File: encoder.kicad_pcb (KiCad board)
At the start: 2 copper layers, 22 x 23.9 mm, 13 parts, among them P1 Molex PicoBlade 6 Right, U1 TLE5012B

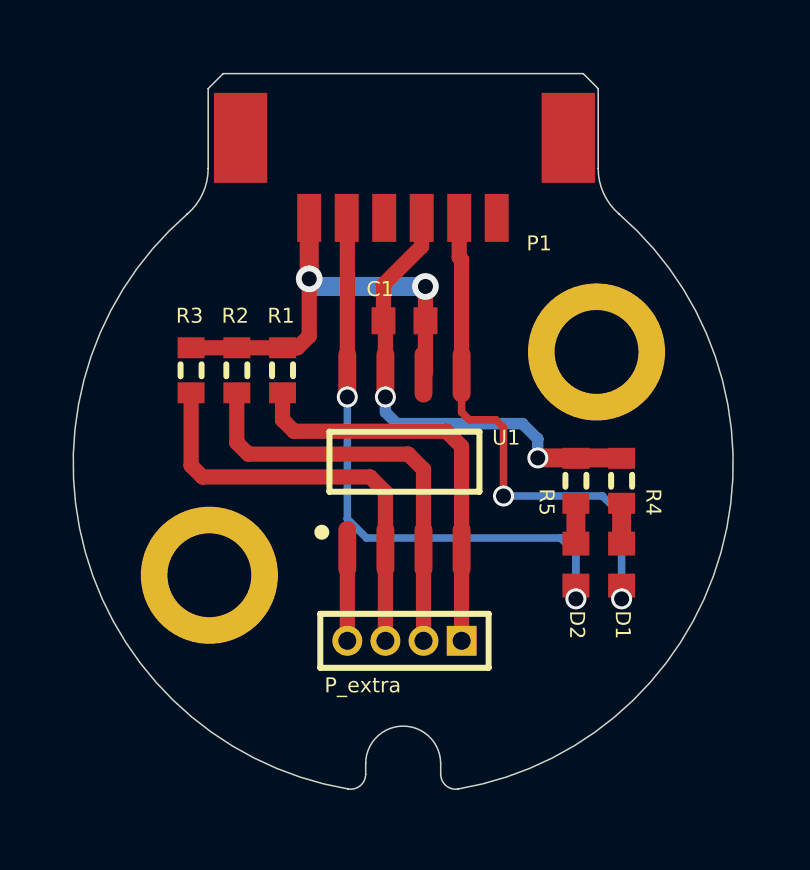
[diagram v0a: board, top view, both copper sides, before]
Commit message: Move to kicad symbols, route INC_C to the main connector.
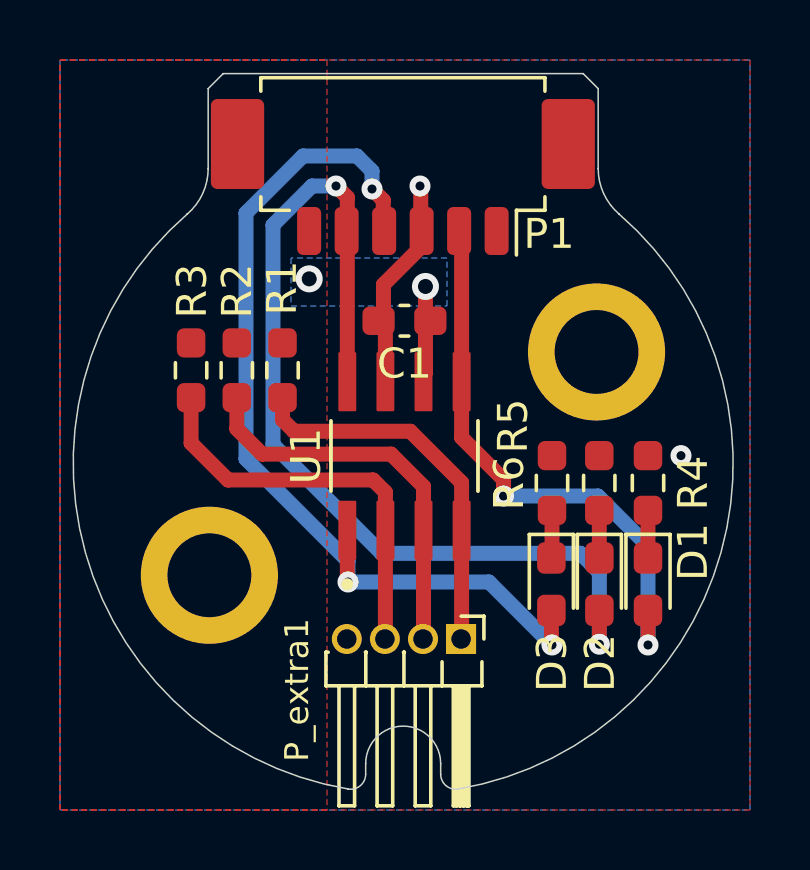
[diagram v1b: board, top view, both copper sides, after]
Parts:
- removed the ? at (142.0, 109.8)
- removed the ? at (154.9, 102.4)
- removed P_extra: MHDR1X4, Miscellaneous Connectors.IntLib:MHDR1X4
- added ?: , , F.Cu at (142.2, 110.1)
- added ?: , , F.Cu at (155.0, 102.4)
- added D3: RED_LED, LED_SMD:LED_0603_1608Metric_Pad1.05x0.95mm_HandSolder, F.Cu at (153.4, 110.1)
- added P_extra1: MHDR1X4, Connector_PinHeader_1.27mm:PinHeader_1x04_P1.27mm_Horizontal, F.Cu at (150.4, 111.9)
- added R6: 1K, Resistor_SMD:R_0603_1608Metric_Pad0.98x0.95mm_HandSolder, F.Cu at (153.5, 106.7)
- C1: value Cap Semi -> 100nF; footprint Miscellaneous Devices.IntLib:1608[0603] -> Capacitor_SMD:C_0603_1608Metric_Pad1.08x0.95mm_HandSolder
- D1, D2: footprint Miscellaneous Devices.IntLib:1608[0603] -> LED_SMD:LED_0603_1608Metric_Pad1.05x0.95mm_HandSolder
- P1: footprint ImmPCB2.IntLib:Molex PicoBlade 6 Right SMD -> 532610671:Molex_PicoBlade_53261-0671_1x06-1MP_P1.25mm_Horizontal
- R1, R2, R3: value Res3 -> 2.2K; footprint Miscellaneous Devices.IntLib:J1-0603 -> Resistor_SMD:R_0603_1608Metric_Pad0.98x0.95mm_HandSolder
- R4, R5: value Res3 -> 1K; footprint Miscellaneous Devices.IntLib:J1-0603 -> Resistor_SMD:R_0603_1608Metric_Pad0.98x0.95mm_HandSolder
- U1: footprint MagneticEncoder.IntLib:SO-8 -> TLE5012BE9000XUMA1:SOIC127P600X175-8N
- moved P1 3.69 mm to (148.5, 95.9), turned to 180 degrees
- moved D1 1.10 mm to (156.7, 110.1), turned to -90 degrees
- moved D2 1.02 mm to (155.0, 110.1), turned to -90 degrees
- moved R4 0.88 mm to (156.7, 106.7)
- moved R5 0.78 mm to (155.0, 106.7)
- moved U1 0.19 mm to (148.5, 105.8)
- turned C1 to 180 degrees
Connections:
- net CSQ renamed /CSQ
- net DATA renamed /DATA
- net SCK renamed /SCK
- C1 pad 1: GND -> +5V
- C1 pad 2: VCC -> GND
- D1 pad 1: INC_A -> Net-(D1-K)
- D1 pad 2: NetD1_2 -> /INC_A
- D2 pad 1: INC_B -> Net-(D2-K)
- D2 pad 2: NetD2_2 -> /INC_B
- P1 pad 1: VCC -> unconnected-(P1-Pin_1-Pad1)
- P1 pad 2: INC_B -> /INC_A
- P1 pad 3: (no net) -> GND
- P1 pad 4: GND -> /INC_C
- P1 pad 5: INC_A -> /INC_B
- P1 pad 6: (no net) -> +5V
- R1 pad 1: VCC -> +5V
- R2 pad 1: VCC -> +5V
- R3 pad 1: VCC -> +5V
- R4 pad 1: NetD1_2 -> Net-(D1-K)
- R5 pad 1: NetD2_2 -> Net-(D2-K)
- U1 pad 1: NetP_extra_4 -> /INC_C
- U1 pad 5: INC_A -> /INC_A
- U1 pad 6: VCC -> +5V
- U1 pad 8: INC_B -> /INC_B
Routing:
- net /INC_B: track 0.00 -> 32.5 mm, vias 0 -> 2
- net /INC_C: track 0.00 -> 31.6 mm, vias 0 -> 3
- net /INC_A: track 0.00 -> 19.4 mm, vias 0 -> 2
- net INC_B: track 18.5 -> 0.00 mm, vias 2 -> 0
- net INC_A: track 17.1 -> 0.00 mm, vias 2 -> 0
- net VCC: track 14.6 -> 0.00 mm, vias 2 -> 0
- net GND: track 14.7 -> 6.82 mm
- net NetP_extra_4: track 3.05 -> 0.00 mm
- net +5V: track 0.00 -> 2.99 mm, vias 0 -> 2
- net Net-(D3-K): track 0.00 -> 1.60 mm
- net Net-(D2-K): track 0.00 -> 1.59 mm
- net Net-(D1-K): track 0.00 -> 1.59 mm
- net NetD2_2: track 1.34 -> 0.00 mm
- net NetD1_2: track 1.34 -> 0.00 mm
- net /DATA: track 13.7 -> 12.8 mm
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- added copper zone on B.Cu, net +5V
- added copper zone on F.Cu, net +5V
- added copper zone on B.Cu, net GND
- added copper zone on F.Cu, net GND
